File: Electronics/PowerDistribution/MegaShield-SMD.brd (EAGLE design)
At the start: 109.2 x 53.3 mm, 37 parts, among them IC1 TLE5206-2G, IC2 TLE5206-2G, IC3 TLE5206-2G, J10 DCJ0202

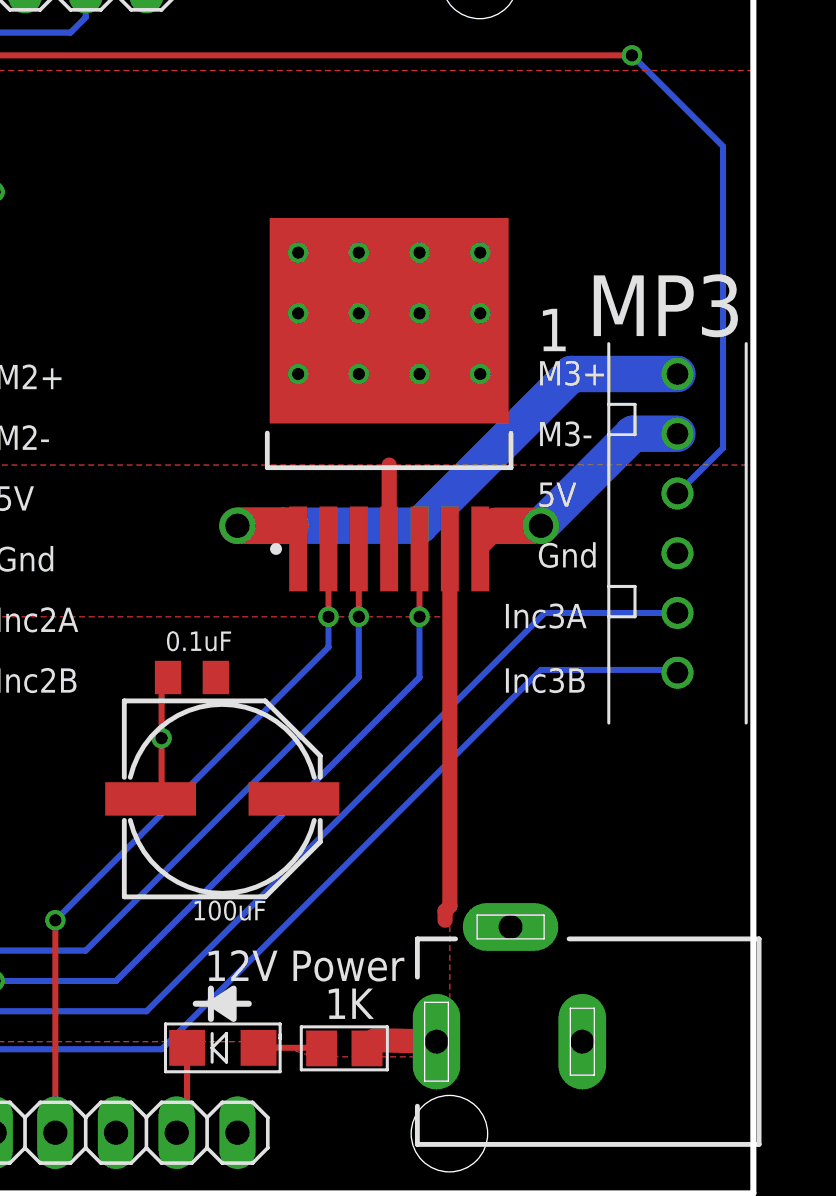
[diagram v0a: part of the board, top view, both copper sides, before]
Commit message: Move MP3 to prevent Inc3B from shorting against USB connector of Arduino Mega
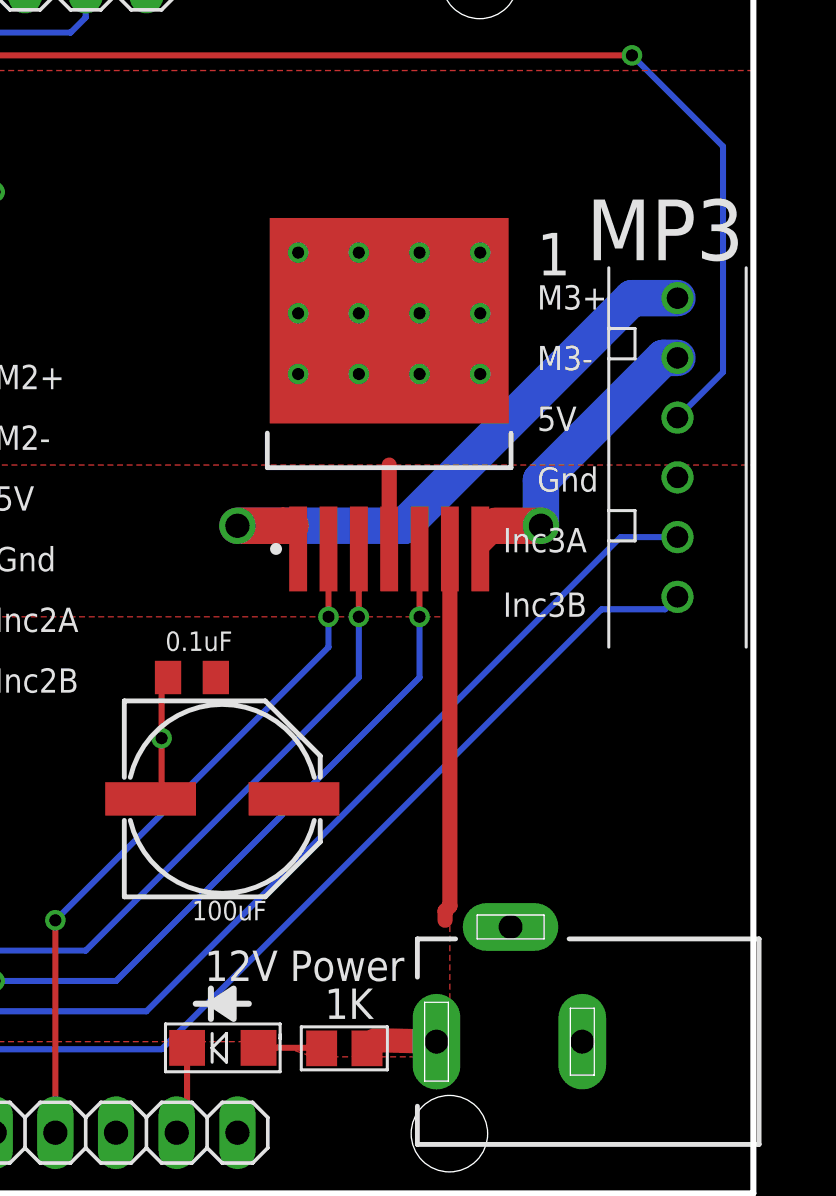
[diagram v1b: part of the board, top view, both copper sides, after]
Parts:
- moved MP3 3.18 mm to (106.0, 37.5)
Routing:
- net 5V: track 193.9 -> 190.7 mm
- net M3-: track 10.4 -> 12.9 mm
- net M3+: track 24.5 -> 25.8 mm
- net INC3A: track 62.5 -> 63.8 mm
- net INC3B: track 59.0 -> 60.2 mm
